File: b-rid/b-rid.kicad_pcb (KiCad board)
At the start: 6 copper layers, 35 x 24 mm, 60 parts, among them J1 USB-C, J2 1S protected pack + NTC, Q1 2N7002P charge isolation, SW1 POWER slide, U1 ESP32-C3-MINI-1-N4X, U2 MIA-M10Q-00B, U3 BQ24074RGT, U4 TPS63031DSK, U5 USBLC6-2SC6, U6 TMUX1119DCKR

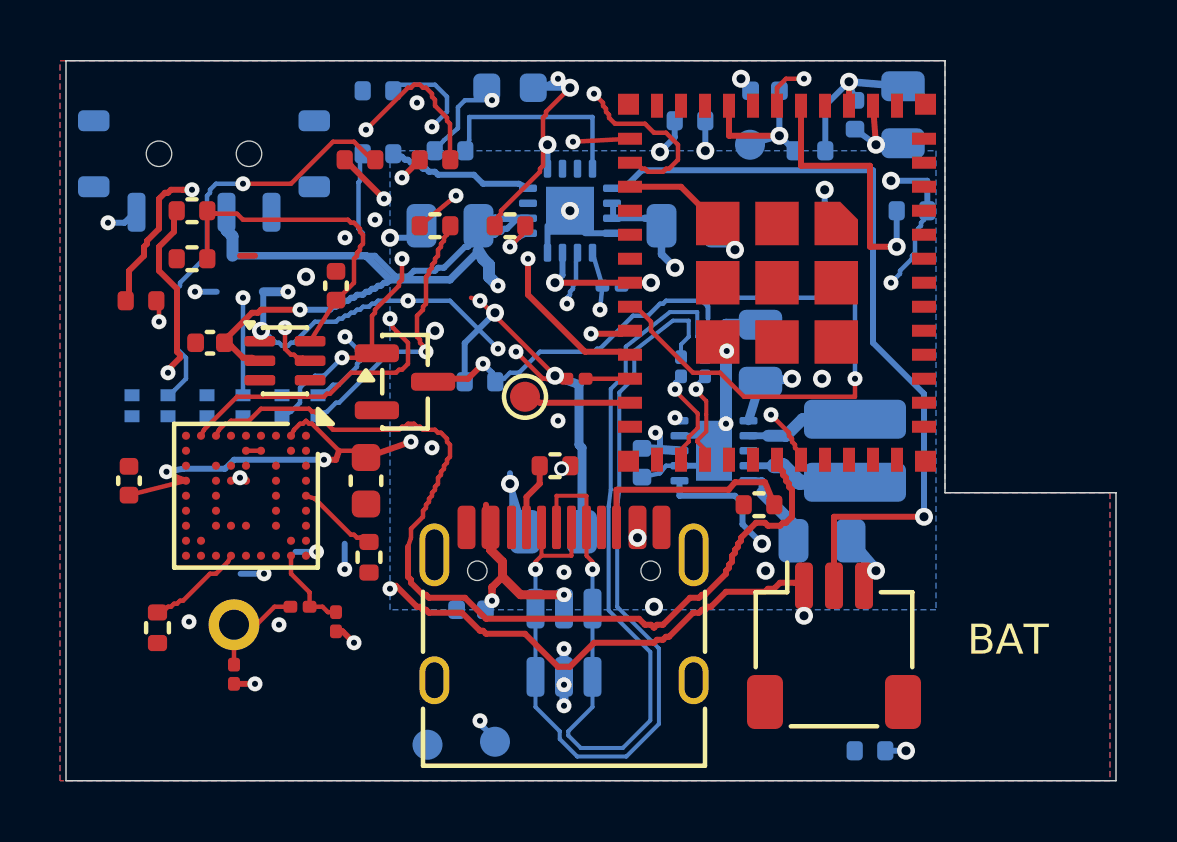
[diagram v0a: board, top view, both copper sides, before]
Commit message: tidied up b-rid nets
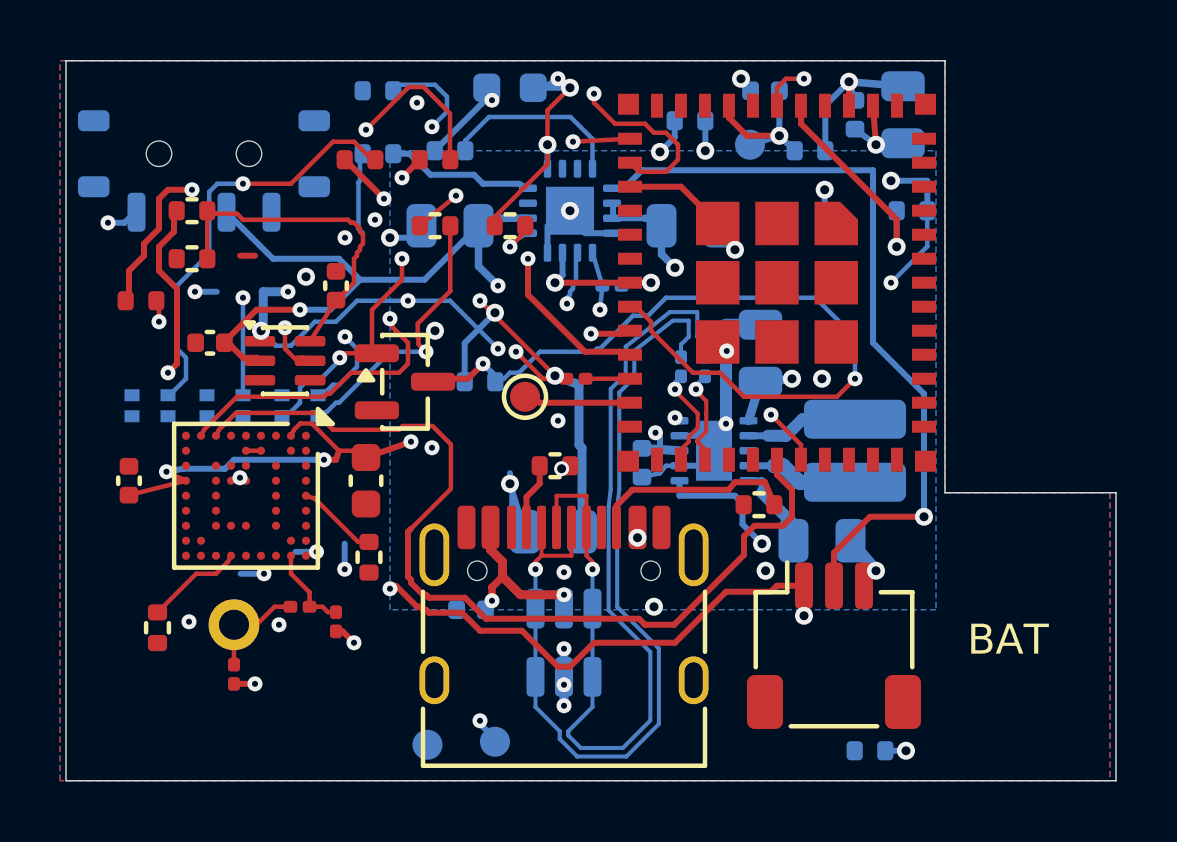
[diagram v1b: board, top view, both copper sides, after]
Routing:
- net /VSYS: track 68.8 -> 60.3 mm
- net /3V3: track 116.6 -> 113.4 mm
- net /BUCK_EN: track 52.1 -> 49.1 mm
- net /VBUS: track 44.7 -> 41.9 mm
- net /BAT+: track 53.6 -> 50.8 mm
- net /CHARGE_ACTIVE: track 29.1 -> 26.8 mm
- net /STRAP_IO2: track 9.09 -> 7.22 mm
- net /ISET: track 6.98 -> 6.20 mm
- net /BATT_NTC: track 26.5 -> 25.8 mm

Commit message: B-RID: tidy power routing and add USB pair rules
Scope: b-rid only. KiCad 10.0.6 native checks: 0/0/0/0; eight negative rule regression tests pass. Engineering prototype CAD for review; fabrication and battery connection are not released.
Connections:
- net /USB_DM renamed /USB_D_N
- net /USB_DM_CONN renamed /USB_D_CONN_N
- net /USB_DP renamed /USB_D_P
- net /USB_DP_CONN renamed /USB_D_CONN_P
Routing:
- net /VSYS: track 60.3 -> 44.7 mm, vias 6 -> 5

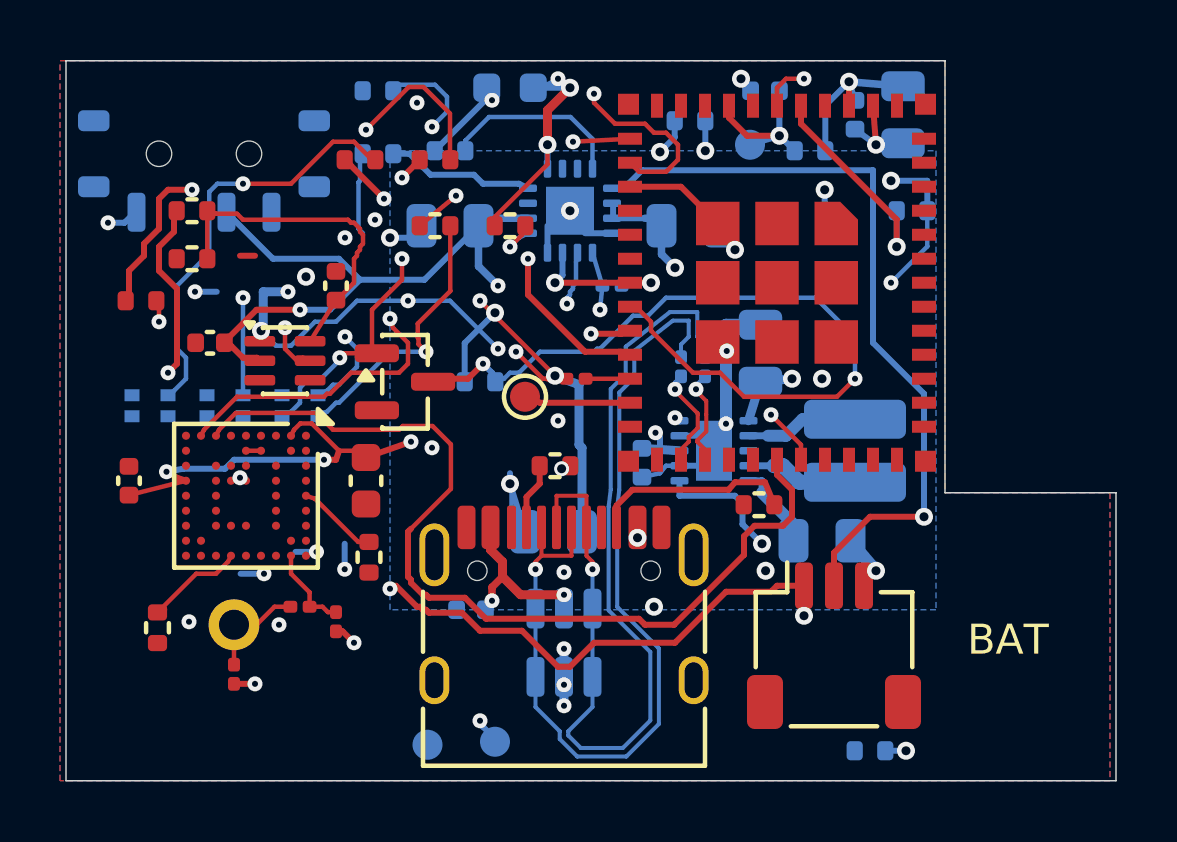
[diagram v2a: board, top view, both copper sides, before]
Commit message: tidied up routes
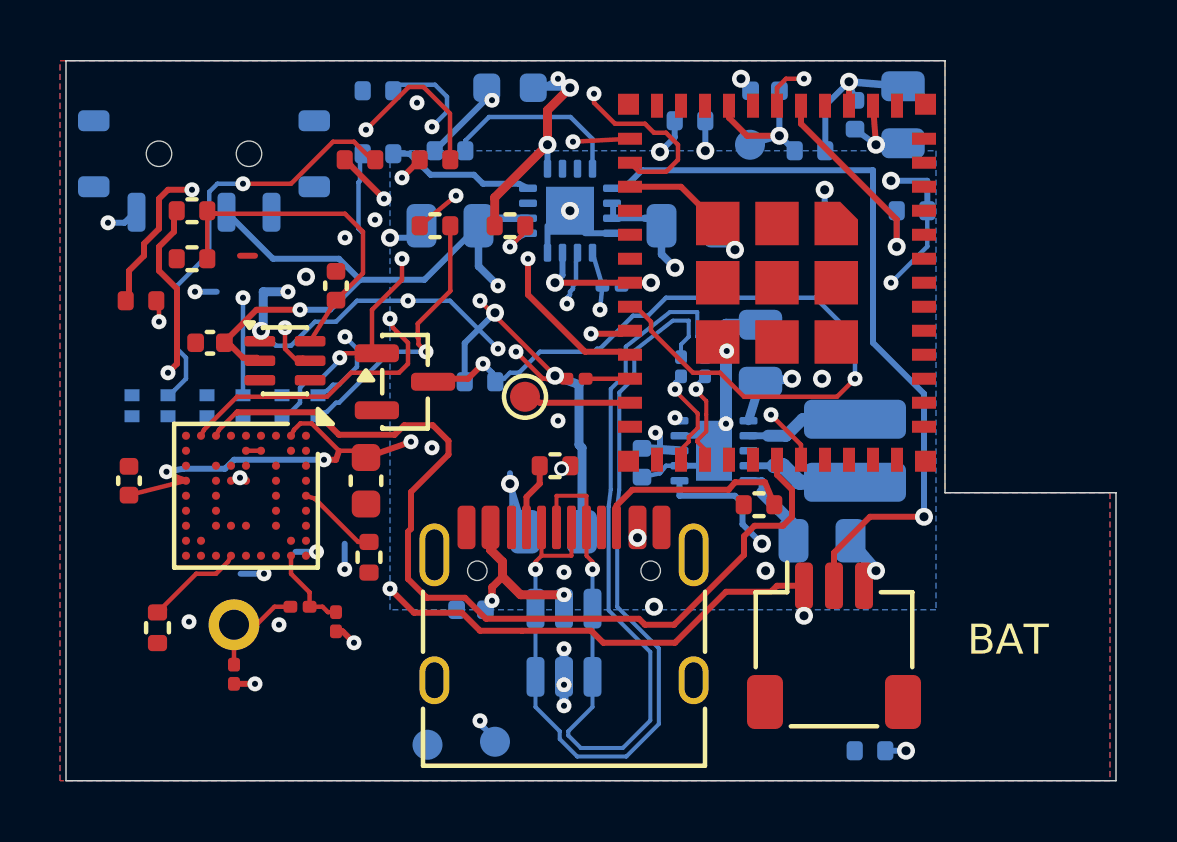
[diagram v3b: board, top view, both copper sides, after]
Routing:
- net /GNSS_TX: track 31.5 -> 34.3 mm
- net /BAT+: track 50.8 -> 50.1 mm
